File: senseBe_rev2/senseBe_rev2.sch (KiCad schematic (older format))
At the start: 33 parts, among them J1 PJ-32434_3-5mmAudioJack, P1 CONN_02X05, Q1 TSM2301, Q2 SI2302, Q3 SI2302, Q4 SI2302, SW1 SW_SPST, SW2 SW_DPST, U1 MDBT42Q, U2 TSSP4056, Y1 T38 Mercury

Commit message: Adds PCB Design and Gerber files.
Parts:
- removed Q2, Q3, Q4: SI2302, Package_TO_SOT_SMD:SOT-23, symbol Transistor_FET:2N7002
- added Q2, Q3: Q_DUAL_NMOS_DMN2990UDJ-7, senseBe_rev2_fp:DMN2990UDJ-7, symbol q_dual_nmos_g1s2g2d2s1d1:Q_DUAL_NMOS_DMN2990UDJ-7
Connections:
- net GND: now also Q2.1 (S), Q2.3 (D), Q3.6 (D)
- net IR_LED_EN: now also U1.18 (P0.05/AIN3); no longer U1.4 (P0.27)
- net LED_GREEN: now also U1.17 (P0.04/AIN2), Q2.5 (G); no longer U1.2 (P0.25)
- net LED_RED: now also U1.16 (P0.03/AIN1), Q2.2 (G); no longer U1.3 (P0.26)
- net LIGHT_SENSE: now also U1.5 (P0.28/AIN4); no longer U1.18 (P0.05/AIN3)
- net PWR1: now also U1.2 (P0.25); no longer U1.16 (P0.03/AIN1)
- net PWR2: now also U1.3 (P0.26); no longer U1.17 (P0.04/AIN2)
- net REG_EN: now also U1.4 (P0.27); no longer U1.5 (P0.28/AIN4)
- net RX_EN: now also Q3.2 (G)
- net at R6.1, U2.2 (GND): now also Q3.1 (S)
- net at R2.1: now also Q2.4 (S)
- net at R3.1: now also Q2.6 (D)
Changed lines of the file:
@@
 Wire Wire Line
 	9950 1650 10225 1650
-$Comp
-L Transistor_FET:2N7002 Q4
-U 1 1 5BA4FCEF
-P 10325 1900
-F 0 "Q4" H 10200 2025 50  0000 L CNN
-F 1 "SI2302" H 10150 1675 50  0000 L CNN
-F 2 "Package_TO_SOT_SMD:SOT-23" H 10525 2000 50  0001 C CNN
-F 3 "~" H 10325 1900 50  0001 C CNN
-	1    10325 1900
-	-1   0    0    -1
-$EndComp
 Wire Wire Line
 	9950 2025 9950 2125
 Text Label 4850 1700 0    50   ~ 0
 LED_RED
-$Comp
-L Transistor_FET:2N7002 Q3
-U 1 1 5BA595BA
-P 6200 1700
-F 0 "Q3" H 6100 1550 50  0000 L CNN
-F 1 "SI2302" H 5975 1450 50  0000 L CNN
-F 2 "Package_TO_SOT_SMD:SOT-23" H 6400 1800 50  0001 C CNN
-F 3 "~" H 6200 1700 50  0001 C CNN
-	1    6200 1700
-	-1   0    0    -1
-$EndComp
-$Comp
-L Transistor_FET:2N7002 Q2
-U 1 1 5BA59F79
-P 5775 1700
-F 0 "Q2" H 5700 1550 50  0000 L CNN
-F 1 "SI2302" H 5575 1450 50  0000 L CNN
-F 2 "Package_TO_SOT_SMD:SOT-23" H 5975 1800 50  0001 C CNN
-F 3 "~" H 5775 1700 50  0001 C CNN
-	1    5775 1700
-	1    0    0    -1
-$EndComp
 Wire Wire Line
 	6100 1150 6100 1500
@@
 	1    0    0    -1
 $EndComp
-NoConn ~ 5400 5225
 NoConn ~ 6100 5225
 NoConn ~ 6200 5225
@@
 Text Label 6000 5925 1    60   ~ 0
 BUTTON
-Text Label 3750 3675 0    60   ~ 0
+Text Label 5500 5925 1    60   ~ 0
 LED_RED
-Text Label 3750 3575 0    60   ~ 0
+Text Label 5600 5925 1    60   ~ 0
 LED_GREEN
-Text Label 4050 4275 0    60   ~ 0
+Text Label 4050 4275 0    50   ~ 0
 DEC4
-Text Label 4050 4375 0    60   ~ 0
+Text Label 4050 4375 0    50   ~ 0
 DCC
 Text Label 7550 3275 2    60   ~ 0
@@
 Text Notes 9225 3050 0    60   ~ 0
 Ambient light sensing
-Text Label 5700 5925 1    50   ~ 0
+Text Label 3750 3875 0    50   ~ 0
 LIGHT_SENSE
 Text Label 5800 5925 1    50   ~ 0
@@
 Wire Wire Line
 	1375 7050 1075 7050
-Text Label 5500 5925 1    50   ~ 0
+Text Label 3750 3575 0    50   ~ 0
 PWR1
-Text Label 5600 5925 1    50   ~ 0
+Text Label 3750 3675 0    50   ~ 0
 PWR2
-Text Label 3750 3775 0    50   ~ 0
+Text Label 5700 5925 1    50   ~ 0
 IR_LED_EN
 Wire Wire Line
@@
 Text Label 9050 6125 0    50   ~ 0
 IR_LED_EN
-Text Label 3750 3875 0    50   ~ 0
+Text Label 3750 3775 0    50   ~ 0
 REG_EN
 Text Label 9050 5900 0    50   ~ 0
@@
 Wire Wire Line
 	3750 3875 4500 3875
-Text Label 3750 3975 0    60   ~ 0
+Text Label 3750 3975 0    50   ~ 0
 LIGHT_SENSE_EN
 Wire Wire Line
@@
 Wire Wire Line
 	5300 1350 5075 1350
+$Comp
+L q_dual_nmos_g1s2g2d2s1d1:Q_DUAL_NMOS_DMN2990UDJ-7 Q2
+U 1 1 5C6CED6D
+P 5775 1700
+F 0 "Q2" H 5575 1800 50  0000 L CNN
+F 1 "Q_DUAL_NMOS_DMN2990UDJ-7" H 5375 1050 50  0000 L CNN
+F 2 "senseBe_rev2_fp:DMN2990UDJ-7" H 5975 1700 50  0001 C CNN
+F 3 "~" H 5975 1700 50  0001 C CNN
+	1    5775 1700
+	1    0    0    -1
+$EndComp
+$Comp
+L q_dual_nmos_g1s2g2d2s1d1:Q_DUAL_NMOS_DMN2990UDJ-7 Q2
+U 2 1 5C6CEE0C
+P 6200 1700
+F 0 "Q2" H 6025 1600 50  0000 L CNN
+F 1 "Q_DUAL_NMOS_DMN2990UDJ-7" H 5875 2250 50  0000 L CNN
+F 2 "senseBe_rev2_fp:DMN2990UDJ-7" H 6400 1700 50  0001 C CNN
+F 3 "~" H 6400 1700 50  0001 C CNN
+	2    6200 1700
+	-1   0    0    1
+$EndComp
+$Comp
+L q_dual_nmos_g1s2g2d2s1d1:Q_DUAL_NMOS_DMN2990UDJ-7 Q3
+U 1 1 5C6E2FF6
+P 10325 1900
+F 0 "Q3" H 10125 2000 50  0000 L CNN
+F 1 "Q_DUAL_NMOS_DMN2990UDJ-7" H 9925 1250 50  0000 L CNN
+F 2 "senseBe_rev2_fp:DMN2990UDJ-7" H 10525 1900 50  0001 C CNN
+F 3 "~" H 10525 1900 50  0001 C CNN
+	1    10325 1900
+	-1   0    0    1
+$EndComp
+NoConn ~ 5400 5225
 $EndSCHEMATC

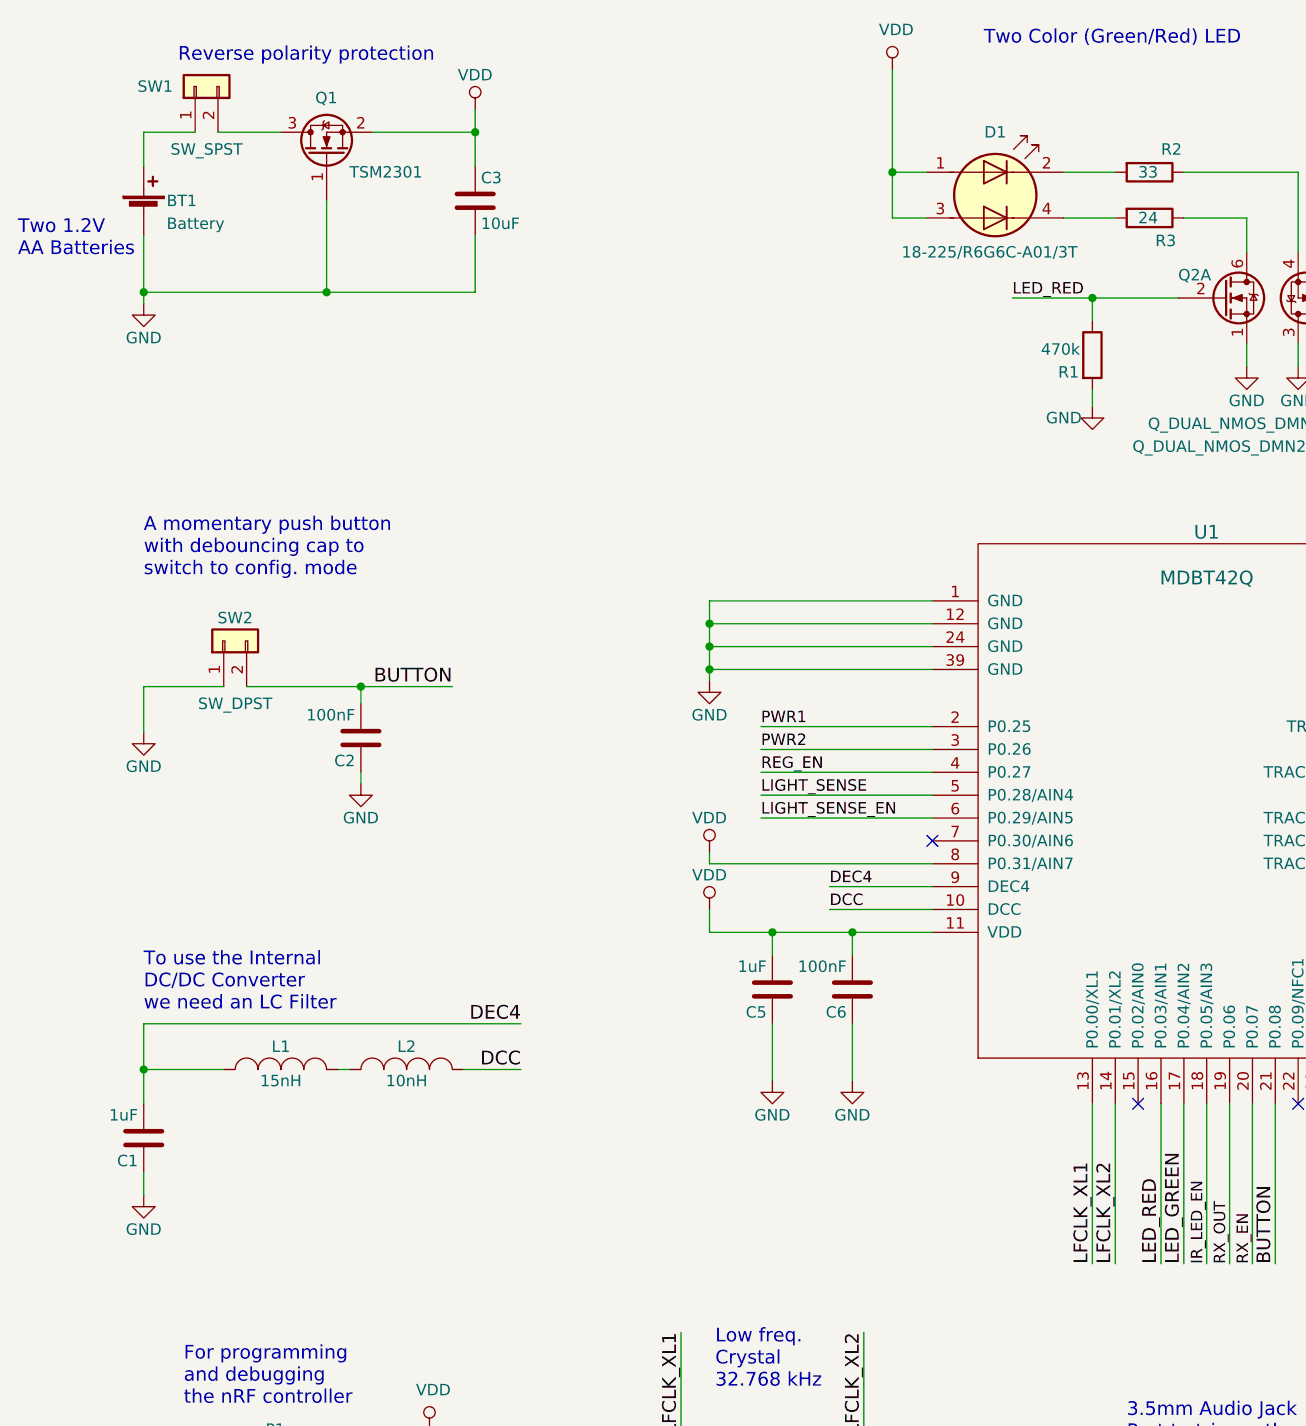
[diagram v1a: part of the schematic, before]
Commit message: senseBe_rev2 PCB and Gerber files modified.
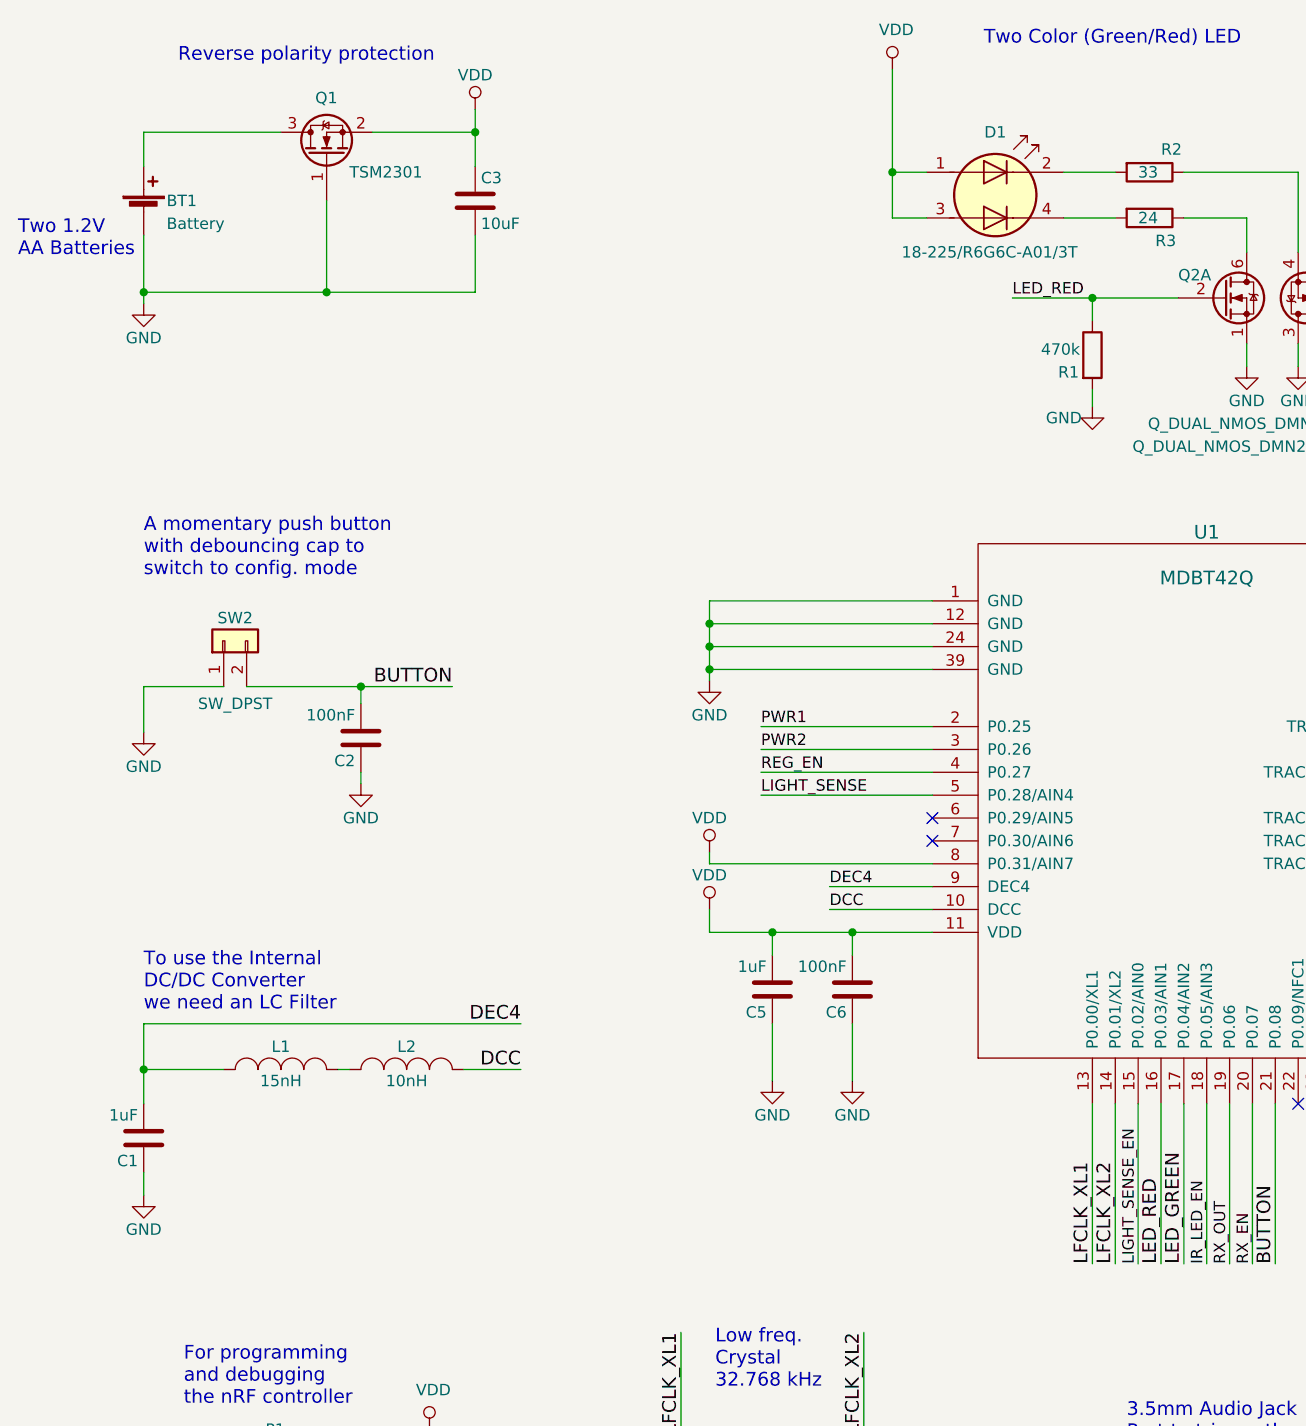
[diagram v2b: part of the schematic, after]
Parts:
- removed SW1: SW_SPST, senseBe_rev2_fp:Molex_KK-6410-02_02x2.54mm_Straight, symbol Connector_Generic:Conn_01x02
- BT1: footprint senseBe_rev2_fp:2462_BatteryHolder_AAx2 -> senseBe_rev2_fp:Molex_KK-6410-02_02x2.54mm_Straight
- MK1, MK2: footprint MountingHole:MountingHole_3mm -> senseBe_rev2_fp:MountingHole_3mm
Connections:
- net LIGHT_SENSE_EN: now also U1.15 (P0.02/AIN0); no longer U1.6 (P0.29/AIN5)
- net at BT1.1 (+): now also Q1.3 (D)
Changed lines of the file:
@@
 F 0 "BT1" H 1150 1375 50  0000 L CNN
 F 1 "Battery" H 1150 1275 50  0000 L CNN
-F 2 "senseBe_rev2_fp:2462_BatteryHolder_AAx2" H 1050 1365 60  0001 C CNN
+F 2 "senseBe_rev2_fp:Molex_KK-6410-02_02x2.54mm_Straight" H 1050 1365 60  0001 C CNN
 F 3 "" V 1050 1365 60  0000 C CNN
 	1    1050 1325
@@
 F 0 "MK1" H 10650 6100 50  0000 C CNN
 F 1 "Mounting_Hole" H 10650 6025 50  0000 C CNN
-F 2 "MountingHole:MountingHole_3mm" H 10650 5900 50  0001 C CNN
+F 2 "senseBe_rev2_fp:MountingHole_3mm" H 10650 5900 50  0001 C CNN
 F 3 "" H 10650 5900 50  0001 C CNN
 	1    10650 5900
@@
 Wire Wire Line
 	6150 7150 6500 7150
-$Comp
-L Connector_Generic:Conn_01x02 SW1
-U 1 1 5C3621CE
-P 1275 775
-F 0 "SW1" V 1275 950 50  0000 C CNN
-F 1 "SW_SPST" V 1000 725 50  0000 C CNN
-F 2 "senseBe_rev2_fp:Molex_KK-6410-02_02x2.54mm_Straight" H 1275 775 50  0001 C CNN
-F 3 "" H 1275 775 50  0001 C CNN
-	1    1275 775
-	0    -1   -1   0
-$EndComp
 Wire Wire Line
 	1050 1675 1850 1675
@@
 F 0 "MK2" H 10650 6450 50  0000 C CNN
 F 1 "Mounting_Hole" H 10650 6375 50  0000 C CNN
-F 2 "MountingHole:MountingHole_3mm" H 10650 6250 50  0001 C CNN
+F 2 "senseBe_rev2_fp:MountingHole_3mm" H 10650 6250 50  0001 C CNN
 F 3 "" H 10650 6250 50  0001 C CNN
 	1    10650 6250
@@
 Wire Wire Line
 	1500 3400 2000 3400
-Wire Wire Line
-	1050 975  1275 975
-Wire Wire Line
-	1375 975  1650 975
 Text Label 1075 7050 0    60   ~ 0
 GPIO2
@@
 Wire Wire Line
 	3750 3875 4500 3875
-Text Label 3750 3975 0    50   ~ 0
+Text Label 5400 5925 1    50   ~ 0
 LIGHT_SENSE_EN
-Wire Wire Line
-	3750 3975 4500 3975
 Wire Wire Line
 	1050 1425 1050 1675
@@
 	-1   0    0    1
 $EndComp
-NoConn ~ 5400 5225
+Wire Wire Line
+	1050 975  1650 975
+Wire Wire Line
+	5400 5925 5400 5225
+NoConn ~ 4500 3975
 $EndSCHEMATC

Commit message: Minor changes of fixing the power Molex connector and traces to Dual MOSFET's SOT963 package.
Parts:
- C1, C2, C3, C4, C5, C6, C7, C8: symbol senseBe_rev1-rescue:C-senseBeRx_rev1-senseBeRx_rev2-rescue-senseBeRx_rev3-rescue-senseBe_rev1-rescue -> senseBe_rev2-rescue:C-senseBeRx_rev1-senseBeRx_rev2-rescue-senseBeRx_rev3-rescue-senseBe_rev1-rescue-senseBe_rev1-rescue
- D1: symbol senseBe_rev1-rescue:LED_Dual_ACAC-senseBeRx_rev1-senseBeRx_rev2-rescue-senseBeRx_rev3-rescue-senseBe_rev1-rescue -> senseBe_rev2-rescue:LED_Dual_ACAC-senseBeRx_rev1-senseBeRx_rev2-rescue-senseBeRx_rev3-rescue-senseBe_rev1-rescue-senseB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
- D2: symbol senseBe_rev1-rescue:D_Photo-senseBeRx_rev1-senseBeRx_rev2-rescue-senseBeRx_rev3-rescue-senseBe_rev1-rescue -> senseBe_rev2-rescue:D_Photo-senseBeRx_rev1-senseBeRx_rev2-rescue-senseBeRx_rev3-rescue-senseBe_rev1-rescue-senseBe_rev1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
- J1: symbol senseBe_rev1:senseBe_rev1_PJ-32434_3-5mmAudioJack -> senseBe_rev2-rescue:senseBe_rev1_PJ-32434_3-5mmAudioJack-senseBe_rev1
- L1, L2: symbol senseBe_rev1-rescue:INDUCTOR_SMALL-senseBeRx_rev1-senseBeRx_rev2-rescue-senseBeRx_rev3-rescue-senseBe_rev1-rescue -> senseBe_rev2-rescue:INDUCTOR_SMALL-senseBeRx_rev1-senseBeRx_rev2-rescue-senseBeRx_rev3-rescue-senseBe_rev1-rescue-sense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
- MK1, MK2: symbol senseBe_rev1-rescue:Mounting_Hole-senseBeRx_rev1-senseBeRx_rev2-rescue-senseBeRx_rev3-rescue-senseBe_rev1-rescue -> senseBe_rev2-rescue:Mounting_Hole-senseBeRx_rev1-senseBeRx_rev2-rescue-senseBeRx_rev3-rescue-senseBe_rev1-rescue-senseB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
- P1: symbol senseBe_rev1-rescue:CONN_02X05-senseBeRx_rev1-senseBeRx_rev2-rescue-senseBeRx_rev3-rescue-senseBe_rev1-rescue -> senseBe_rev2-rescue:CONN_02X05-senseBeRx_rev1-senseBeRx_rev2-rescue-senseBeRx_rev3-rescue-senseBe_rev1-rescue-senseBe_r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
- Q2, Q3: symbol q_dual_nmos_g1s2g2d2s1d1:Q_DUAL_NMOS_DMN2990UDJ-7 -> senseBe_rev2-rescue:Q_DUAL_NMOS_DMN2990UDJ-7-q_dual_nmos_g1s2g2d2s1d1
- R1, R2, R3, R4, R5, R6, R7: symbol senseBe_rev1-rescue:R-senseBeRx_rev1-senseBeRx_rev2-rescue-senseBeRx_rev3-rescue-senseBe_rev1-rescue -> senseBe_rev2-rescue:R-senseBeRx_rev1-senseBeRx_rev2-rescue-senseBeRx_rev3-rescue-senseBe_rev1-rescue-senseBe_rev1-rescue
- U1: symbol senseBe_rev1-rescue:MDBT42Q-senseBeRx_rev1-senseBeRx_rev2-rescue-senseBeRx_rev3-rescue-senseBe_rev1-rescue -> senseBe_rev2-rescue:MDBT42Q-senseBeRx_rev1-senseBeRx_rev2-rescue-senseBeRx_rev3-rescue-senseBe_rev1-rescue-senseBe_rev1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
- U2: symbol senseBe_rev1-rescue:TSSP40xx-senseBeRx_rev1-senseBeRx_rev2-rescue-senseBeRx_rev3-rescue-senseBe_rev1-rescue -> senseBe_rev2-rescue:TSSP40xx-senseBeRx_rev1-senseBeRx_rev2-rescue-senseBeRx_rev3-rescue-senseBe_rev1-rescue-senseBe_rev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
- Y1: symbol senseBe_rev1-rescue:Crystal-senseBeRx_rev1-senseBeRx_rev2-rescue-senseBeRx_rev3-rescue-senseBe_rev1-rescue -> senseBe_rev2-rescue:Crystal-senseBeRx_rev1-senseBeRx_rev2-rescue-senseBeRx_rev3-rescue-senseBe_rev1-rescue-senseBe_rev1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
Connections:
- net BUTTON: now also SW2.1 (Pin_1); no longer SW2.2 (Pin_2)
- net GND: now also SW2.2 (Pin_2); no longer SW2.1 (Pin_1)
